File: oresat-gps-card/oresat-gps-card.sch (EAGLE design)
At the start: 372 parts, among them J1 ORESAT-DEBUG-CONNECTOR-CARD, J100 DM3BT-DSF-PEJS, J102 FTSH-105-XX-X-DV-K, J4 TFM-120-01-L-D-RA, Q1 MMBT2907, Q2 PMV45EN, Q3 DMP2240UDM, Q4 PMV45EN, Q5 MOSFET-PCH-SOT23-6, Q6 MOSFET-PCH-SOT23-6, U1 RCLAMP0504FB, U10 TLVH431, U11 TCAN330, U12 MIC842LYC5, U13 MIC842LYC5, U14 MAX4211FETE, U15 TPS62112, U16 MAX7310ATE, U17 25AAXX, U18 RCLAMP0504FB, U19 BP2G+, U2 TPS2051CDBVR, U20 MAX8510EXK29+T, U22 LT1719S6, U4 SN74LVC1G07DCK, U5 SKY65723-81, U6 7Q-16.368MBG-T, U7 OSD3358-512M-BSM, U8 MAX8510EXK29+T, U9 MAX8510EXK29+T, Y1 24MHz, Y2 ABS07-32.768KHZ-T

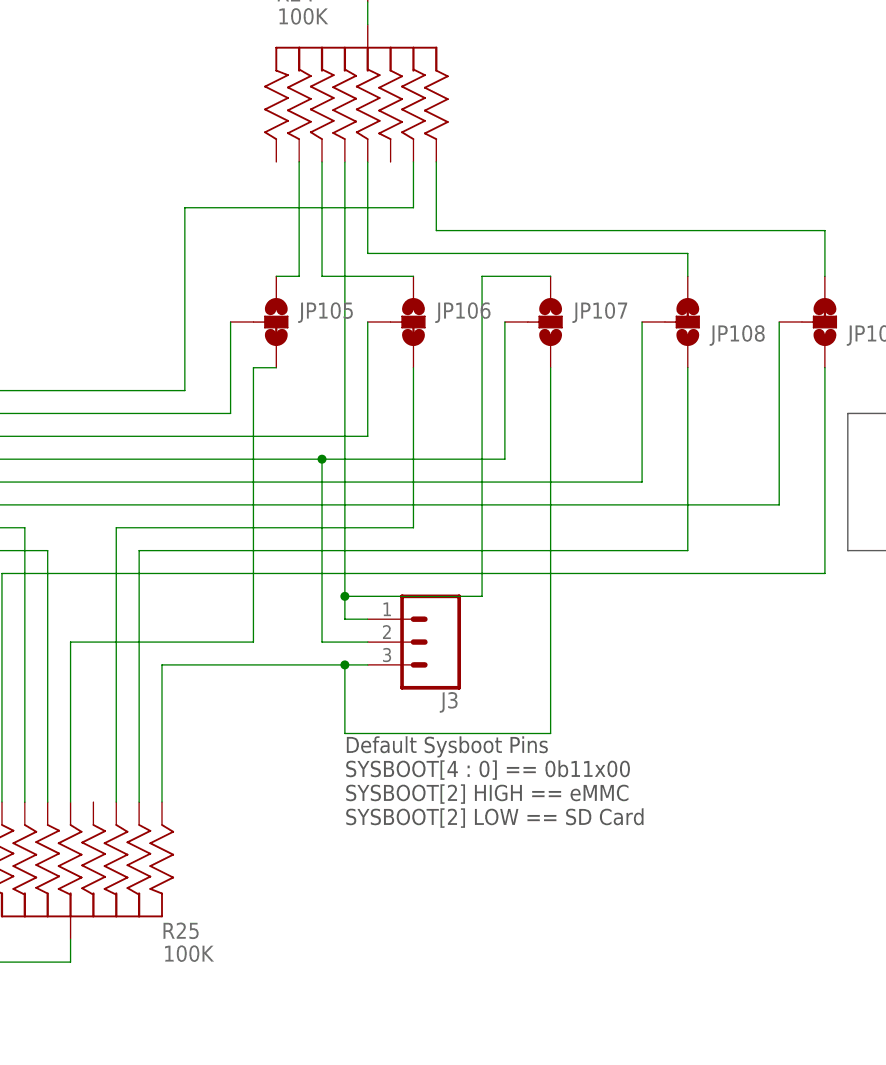
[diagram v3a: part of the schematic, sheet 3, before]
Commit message: Updated boot circuitry. Cleaned up names layer.
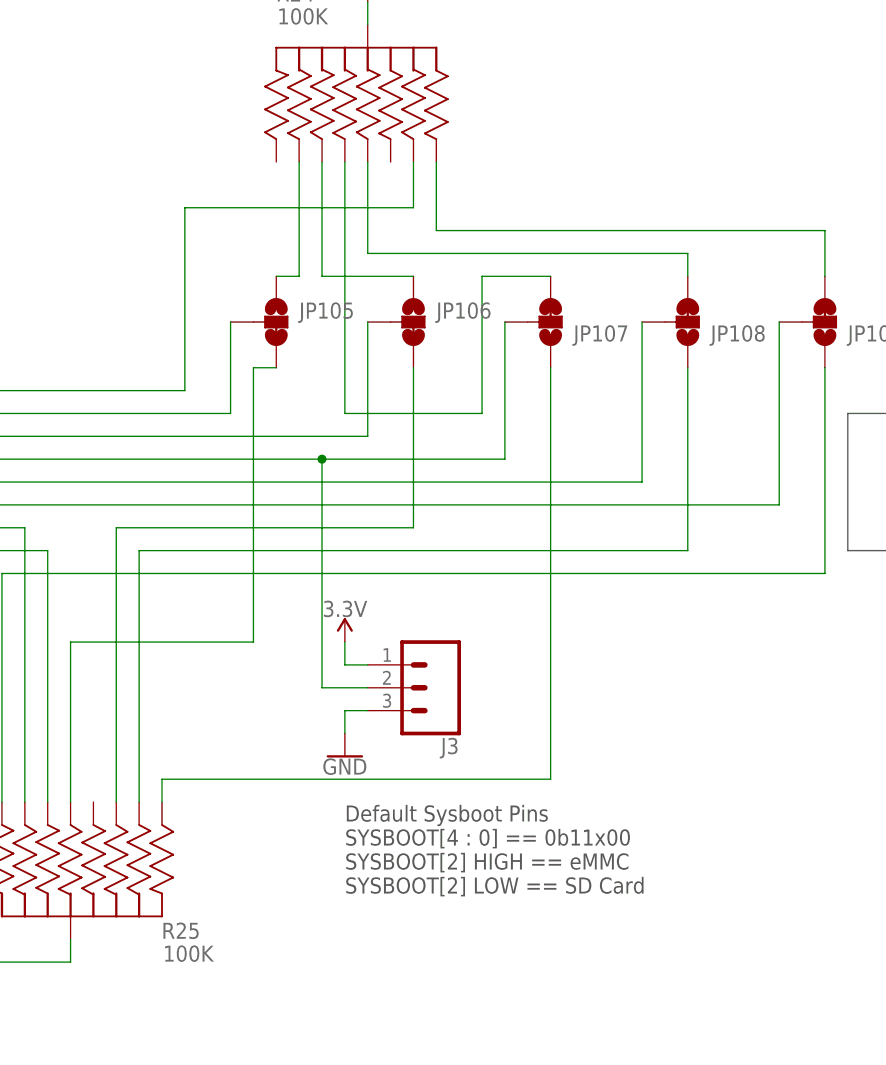
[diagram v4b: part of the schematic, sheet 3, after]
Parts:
- JP107: value JUMPER-SMT_3_NO_SILK -> JUMPER-SMT_3_1-NC_TRACE_SILK; device SparkFun-Jumpers:JUMPER-SMT_3_NO_SILK -> SparkFun-Jumpers:JUMPER-SMT_3_1-NC_TRACE_SILK
- L8: value SF14-1575F5UU19 -> SF14-1575F5UUA1
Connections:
- net 3.3V: now also J3.1
- net GND: now also J3.3
- net N$109: now also JP107.3; no longer J3.1, JP107.1
- net N$631: now also JP107.1; no longer J3.3, JP107.3
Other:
- moved on the sheet: J3
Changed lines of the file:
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@@
 <setting verticaltext="up"/>
 </settings>
-<grid distance="0.05" unitdist="inch" unit="inch" style="lines" multiple="1" display="no" altdistance="0.01" altunitdist="inch" altunit="inch"/>
+<grid distance="0.1" unitdist="inch" unit="inch" style="lines" multiple="1" display="no" altdistance="0.01" altunitdist="inch" altunit="inch"/>
 <layers>
 <layer number="1" name="Top" color="4" fill="1" visible="no" active="no"/>
@@
 <part name="GND35" library="SparkFun-PowerSymbols" deviceset="GND" device=""/>
 <part name="J3" library="SparkFun-Connectors" deviceset="CONN_03" device="LONGPADS" package3d_urn="urn:adsk.eagle:package:38068/1"/>
-<part name="JP105" library="SparkFun-Jumpers" deviceset="JUMPER-SMT_3_1-NC_TRACE" device="_SILK"/>
-<part name="JP106" library="SparkFun-Jumpers" deviceset="JUMPER-SMT_3_1-NC_TRACE" device="_SILK"/>
-<part name="JP108" library="SparkFun-Jumpers" deviceset="JUMPER-SMT_3_1-NC_TRACE" device="_SILK"/>
-<part name="JP107" library="SparkFun-Jumpers" deviceset="JUMPER-SMT_3_NO" device="_SILK"/>
-<part name="JP109" library="SparkFun-Jumpers" deviceset="JUMPER-SMT_3_1-NC_TRACE" device="_SILK"/>
+<part name="JP105" library="SparkFun-Jumpers" deviceset="JUMPER-SMT_3_1-NC_TRACE" device="_SILK" package3d_urn="urn:adsk.eagle:package:39288/1"/>
+<part name="JP106" library="SparkFun-Jumpers" deviceset="JUMPER-SMT_3_1-NC_TRACE" device="_SILK" package3d_urn="urn:adsk.eagle:package:39288/1"/>
+<part name="JP108" library="SparkFun-Jumpers" deviceset="JUMPER-SMT_3_1-NC_TRACE" device="_SILK" package3d_urn="urn:adsk.eagle:package:39288/1"/>
+<part name="JP107" library="SparkFun-Jumpers" deviceset="JUMPER-SMT_3_1-NC_TRACE" device="_SILK" package3d_urn="urn:adsk.eagle:package:39288/1"/>
+<part name="JP109" library="SparkFun-Jumpers" deviceset="JUMPER-SMT_3_1-NC_TRACE" device="_SILK" package3d_urn="urn:adsk.eagle:package:39288/1"/>
 <part name="TP142" library="SparkFun-Connectors" deviceset="TEST-POINT" device="3X4" package3d_urn="urn:adsk.eagle:package:38287/1"/>
 <part name="TP146" library="SparkFun-Connectors" deviceset="TEST-POINT" device="3X4" package3d_urn="urn:adsk.eagle:package:38287/1"/>
@@
 <part name="GND40" library="SparkFun-Aesthetics" deviceset="GND" device=""/>
 <part name="C57" library="oresat-rcl" deviceset="C-EU" device="0603-B-NOSILK" value="100p"/>
-<part name="L8" library="saw_1.4x1.1" deviceset="SAW_1.4X1.1" device="" value="SF14-1575F5UU19"/>
+<part name="L8" library="saw_1.4x1.1" deviceset="SAW_1.4X1.1" device="" value="SF14-1575F5UUA1"/>
 <part name="C51" library="oresat-rcl" deviceset="C-EU" device="0603-B-NOSILK" value="100n"/>
 <part name="C53" library="oresat-rcl" deviceset="C-EU" device="0603-B-NOSILK" value="2.2u"/>
@@
 <part name="GND4" library="supply1" library_urn="urn:adsk.eagle:library:371" deviceset="GND" device=""/>
 <part name="TP71" library="SparkFun-Connectors" deviceset="TEST-POINT" device="3X4" package3d_urn="urn:adsk.eagle:package:38287/1"/>
+<part name="GND5" library="SparkFun-PowerSymbols" deviceset="GND" device=""/>
+<part name="3V-6" library="oresat-supplies" deviceset="3.3V" device=""/>
 </parts>
 <sheets>
@@
 <wire x1="478.155" y1="337.82" x2="478.155" y2="325.12" width="0.1524" layer="97"/>
 <wire x1="478.155" y1="325.12" x2="469.9" y2="325.12" width="0.1524" layer="97"/>
-<text x="718.82" y="342.9" size="1.778" layer="97">Default Sysboot Pins
+<text x="718.82" y="335.28" size="1.778" layer="97">Default Sysboot Pins
 SYSBOOT[4 : 0] == 0b11x00
 SYSBOOT[2] HIGH == eMMC
@@
 <attribute name="VALUE" x="473.456" y="328.549" size="1.778" layer="96"/>
 </instance>
-<instance part="J3" gate="J$1" x="728.98" y="363.22" smashed="yes" rot="R180">
-<attribute name="VALUE" x="731.52" y="370.586" size="1.778" layer="96" font="vector" rot="R180"/>
-<attribute name="NAME" x="731.52" y="357.632" size="1.778" layer="95" font="vector" rot="R180"/>
+<instance part="J3" gate="J$1" x="728.98" y="358.14" smashed="yes" rot="R180">
+<attribute name="VALUE" x="731.52" y="365.506" size="1.778" layer="96" font="vector" rot="R180"/>
+<attribute name="NAME" x="731.52" y="352.552" size="1.778" layer="95" font="vector" rot="R180"/>
 </instance>
 <instance part="JP105" gate="G$1" x="711.2" y="398.78" smashed="yes">
@@
 <attribute name="NAME" x="759.46" y="398.399" size="1.778" layer="95" font="vector" rot="MR180"/>
 </instance>
-<instance part="JP107" gate="G$1" x="741.68" y="398.78" smashed="yes">
-<attribute name="NAME" x="744.22" y="399.161" size="1.778" layer="95" font="vector"/>
+<instance part="JP107" gate="G$1" x="741.68" y="398.78" smashed="yes" rot="MR180">
+<attribute name="NAME" x="744.22" y="398.399" size="1.778" layer="95" font="vector" rot="MR180"/>
 </instance>
 <instance part="JP109" gate="G$1" x="772.16" y="398.78" smashed="yes" rot="MR180">
@@
 <attribute name="NAME" x="282.448" y="310.642" size="1.778" layer="95" font="vector" rot="R180"/>
 </instance>
+<instance part="GND5" gate="1" x="718.82" y="350.52" smashed="yes">
+<attribute name="VALUE" x="718.82" y="350.266" size="1.778" layer="96" align="top-center"/>
+</instance>
+<instance part="3V-6" gate="G$1" x="718.82" y="365.76" smashed="yes">
+<attribute name="VALUE" x="718.82" y="366.014" size="1.778" layer="96" align="bottom-center"/>
+</instance>
 </instances>
 <busses>
@@
 <wire x1="162.56" y1="457.2" x2="162.56" y2="459.74" width="0.1524" layer="91"/>
 </segment>
+<segment>
+<pinref part="J3" gate="J$1" pin="1"/>
+<wire x1="721.36" y1="360.68" x2="718.82" y2="360.68" width="0.1524" layer="91"/>
+<wire x1="718.82" y1="360.68" x2="718.82" y2="363.22" width="0.1524" layer="91"/>
+<pinref part="3V-6" gate="G$1" pin="3.3V"/>
+</segment>
 </net>
 <net name="N$535" class="0">
@@
 <wire x1="635" y1="383.54" x2="716.28" y2="383.54" width="0.1524" layer="91"/>
 <pinref part="U7" gate="D" pin="LCD_DATA2"/>
-<wire x1="716.28" y1="383.54" x2="716.28" y2="363.22" width="0.1524" layer="91"/>
+<wire x1="716.28" y1="383.54" x2="716.28" y2="358.14" width="0.1524" layer="91"/>
 <pinref part="J3" gate="J$1" pin="2"/>
-<wire x1="716.28" y1="363.22" x2="721.36" y2="363.22" width="0.1524" layer="91"/>
+<wire x1="716.28" y1="358.14" x2="721.36" y2="358.14" width="0.1524" layer="91"/>
 <wire x1="716.28" y1="383.54" x2="736.6" y2="383.54" width="0.1524" layer="91"/>
 <wire x1="736.6" y1="383.54" x2="736.6" y2="398.78" width="0.1524" layer="91"/>
@@
 <net name="N$631" class="0">
 <segment>
-<wire x1="698.5" y1="345.44" x2="698.5" y2="360.68" width="0.1524" layer="91"/>
+<wire x1="698.5" y1="345.44" x2="698.5" y2="347.98" width="0.1524" layer="91"/>
 <pinref part="R25" gate="A" pin="11"/>
-<pinref part="J3" gate="J$1" pin="3"/>
-<wire x1="698.5" y1="360.68" x2="718.82" y2="360.68" width="0.1524" layer="91"/>
-<wire x1="718.82" y1="360.68" x2="721.36" y2="360.68" width="0.1524" layer="91"/>
-<wire x1="741.68" y1="393.7" x2="741.68" y2="353.06" width="0.1524" layer="91"/>
-<wire x1="741.68" y1="353.06" x2="718.82" y2="353.06" width="0.1524" layer="91"/>
-<wire x1="718.82" y1="353.06" x2="718.82" y2="360.68" width="0.1524" layer="91"/>
-<junction x="718.82" y="360.68"/>
-<pinref part="JP107" gate="G$1" pin="3"/>
+<wire x1="741.68" y1="347.98" x2="698.5" y2="347.98" width="0.1524" layer="91"/>
+<pinref part="JP107" gate="G$1" pin="1"/>
+<wire x1="741.68" y1="347.98" x2="741.68" y2="393.7" width="0.1524" layer="91"/>
 </segment>
 </net>
@@
 <net name="N$109" class="0">
 <segment>
-<pinref part="J3" gate="J$1" pin="1"/>
-<wire x1="721.36" y1="365.76" x2="718.82" y2="365.76" width="0.1524" layer="91"/>
-<wire x1="718.82" y1="365.76" x2="718.82" y2="368.3" width="0.1524" layer="91"/>
 <pinref part="R24" gate="A" pin="88"/>
-<wire x1="718.82" y1="368.3" x2="718.82" y2="416.56" width="0.1524" layer="91"/>
-<wire x1="718.82" y1="368.3" x2="734.06" y2="368.3" width="0.1524" layer="91"/>
-<wire x1="734.06" y1="368.3" x2="734.06" y2="403.86" width="0.1524" layer="91"/>
-<junction x="718.82" y="368.3"/>
+<wire x1="718.82" y1="388.62" x2="718.82" y2="416.56" width="0.1524" layer="91"/>
+<wire x1="718.82" y1="388.62" x2="734.06" y2="388.62" width="0.1524" layer="91"/>
+<wire x1="734.06" y1="388.62" x2="734.06" y2="403.86" width="0.1524" layer="91"/>
+<pinref part="JP107" gate="G$1" pin="3"/>
 <wire x1="734.06" y1="403.86" x2="741.68" y2="403.86" width="0.1524" layer="91"/>
-<pinref part="JP107" gate="G$1" pin="1"/>
 </segment>
 </net>
@@
 <wire x1="162.56" y1="436.88" x2="162.56" y2="434.34" width="0.1524" layer="91"/>
 </segment>
+<segment>
+<pinref part="J3" gate="J$1" pin="3"/>
+<wire x1="721.36" y1="355.6" x2="718.82" y2="355.6" width="0.1524" layer="91"/>
+<wire x1="718.82" y1="355.6" x2="718.82" y2="353.06" width="0.1524" layer="91"/>
+<pinref part="GND5" gate="1" pin="GND"/>
+</segment>
 </net>

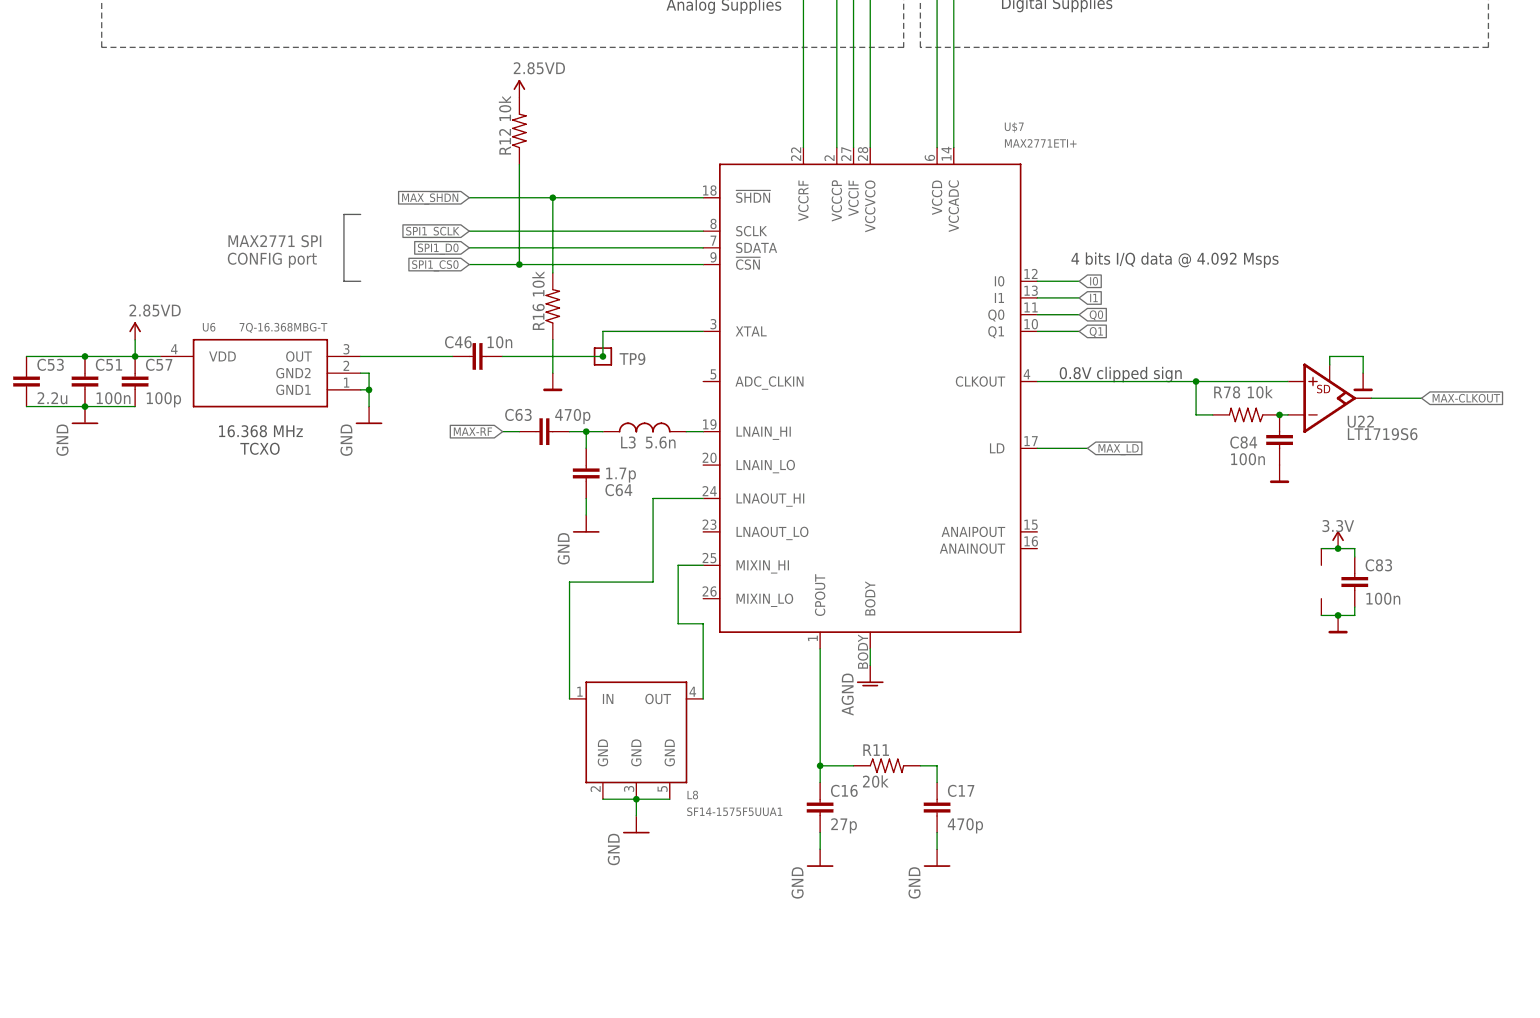
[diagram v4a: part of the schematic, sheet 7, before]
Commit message: Fixed design review things: made net names more clear, removed solder mask from top of RF traces, opened up space around octavo 3.3v pads, moved digital LDO for the max chip, added pin header and through hole testpoints for GPS lines. Some other small changes.
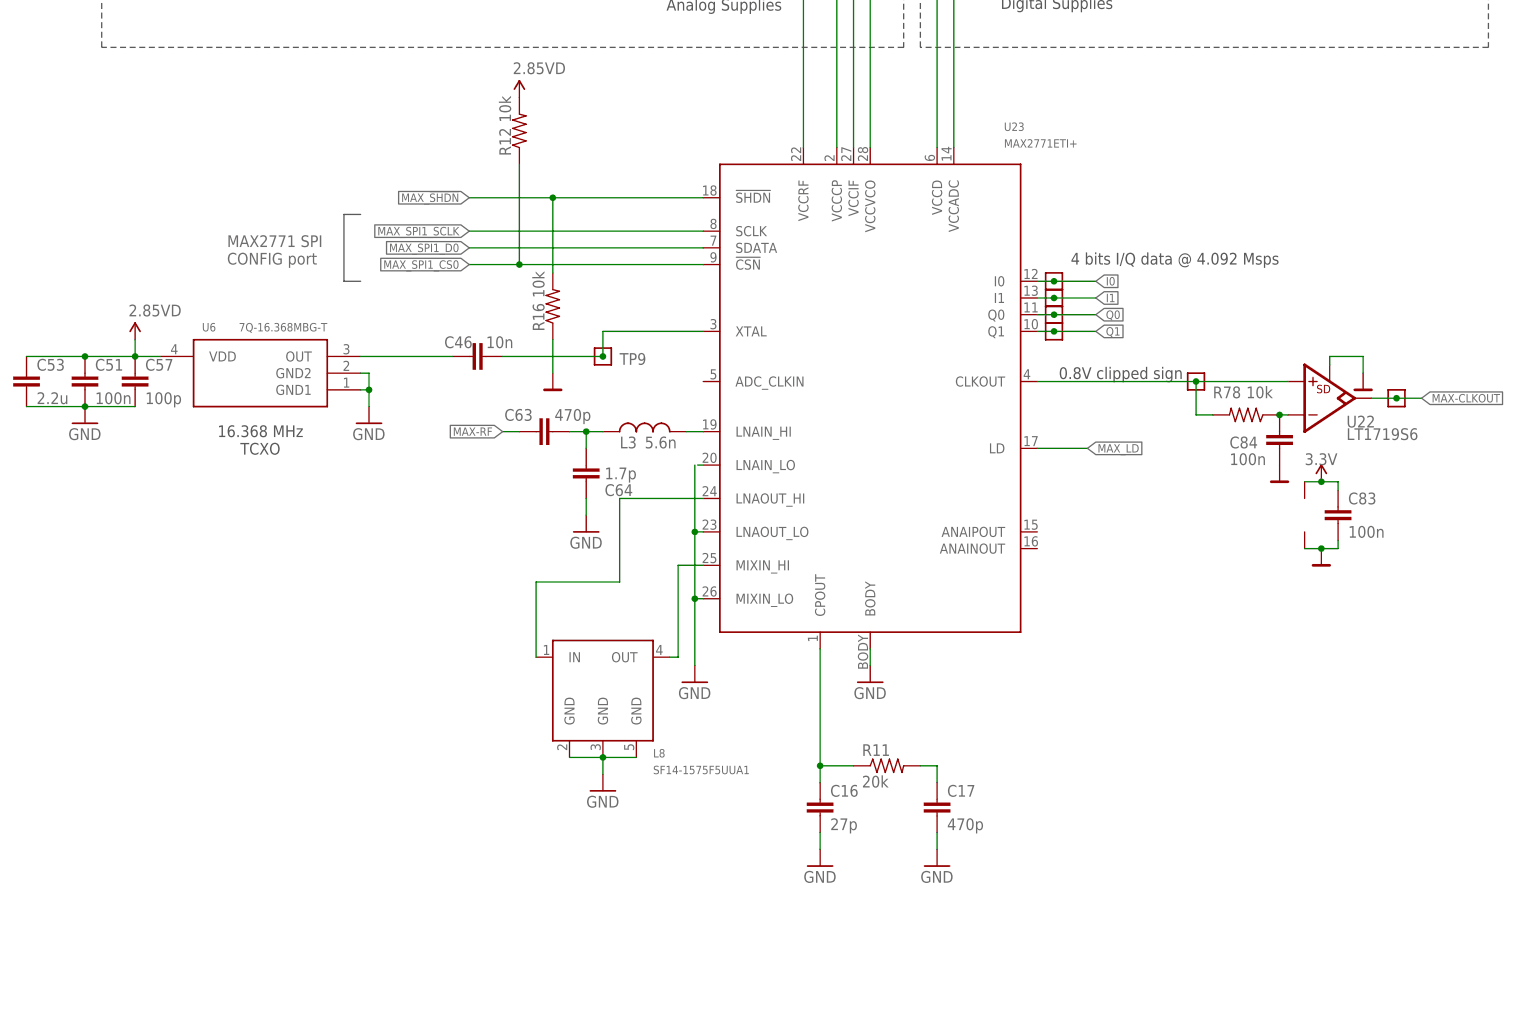
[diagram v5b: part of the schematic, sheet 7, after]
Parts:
- removed TP10, TP143, TP36, TP37: TEST-POINT3X4, SparkFun-Connectors:TEST-POINT3X4
- added C65: 100n, oresat-rcl:C-EU0603-B-NOSILK
- added JP2: (no value), pinhead:PINHD-1X6
- added TP72: TEST-POINT-LARGE-SQUARE, oresat-misc:TEST-POINT-LARGE-SQUARE
- TP20, TP21, TP33, TP34, TP71: value TEST-POINT3X4 -> TEST-POINT-LARGE-SQUARE; device SparkFun-Connectors:TEST-POINT3X4 -> oresat-misc:TEST-POINT-LARGE-SQUARE
- U3: value (none) -> THGBMJG7C2LBAU8
- renumbered U$7 to U23
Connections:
- removed net SPI1_CS0: R12.1, TP143.1, U23.!CSN, U7D.RMII1_REF_CLK
- removed net SPI1_D0: TP36.1, U23.SDATA, U7D.MII1_CRS
- removed net SPI1_SCLK: TP37.1, U23.SCLK, U7D.MII1_COL
- removed net UART2_RX: R18.1, TP147.1, TP27.1, U7D.MII1_TX_CLK
- removed net UART2_TX: R14.1, TP10.1, TP6.1, U7D.MII1_RX_CLK
- new net MAX_SPI1_CS0: JP2.3, R12.1, U23.!CSN, U7D.RMII1_REF_CLK
- new net MAX_SPI1_D0: JP2.5, U23.SDATA, U7D.MII1_CRS
- new net MAX_SPI1_SCLK: JP2.4, U23.SCLK, U7D.MII1_COL
- new net STQ_UART2_RX: JP2.2, R18.1, TP147.1, TP27.1, U7D.MII1_TX_CLK
- new net STQ_UART2_TX: JP2.1, R14.1, TP6.1, U7D.MII1_RX_CLK
- net 2.85VD: now also C65.1
- net GND: now also C65.2, JP2.6, U23.LNAIN_LO, U23.LNAOUT_LO, U23.MIXIN_LO
- net I0: now also TP20.1; no longer TP21.1
- net I1: now also TP21.1; no longer TP20.1
- net MAX-CLKOUT: now also TP72.1; no longer TP71.1
- net MAX_CLK_OUT: now also TP71.1
- net Q0: now also TP33.1; no longer TP34.1
- net Q1: now also TP34.1; no longer TP33.1
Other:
- moved on the sheet: C59, C83, L8, TP148, TP5
